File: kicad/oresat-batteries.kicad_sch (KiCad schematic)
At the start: 11 parts, among them J1 J-SAMTEC-TFM-120-X1-XXX-D-RA, SW1 Omron D2F-L3-D (LEFT), SW2 Omron D2F-L3-D (RIGHT), SW3 OMRON D2F-L3-D (LEFT), SW4 OMRON D2F-L3-D (RIGHT)

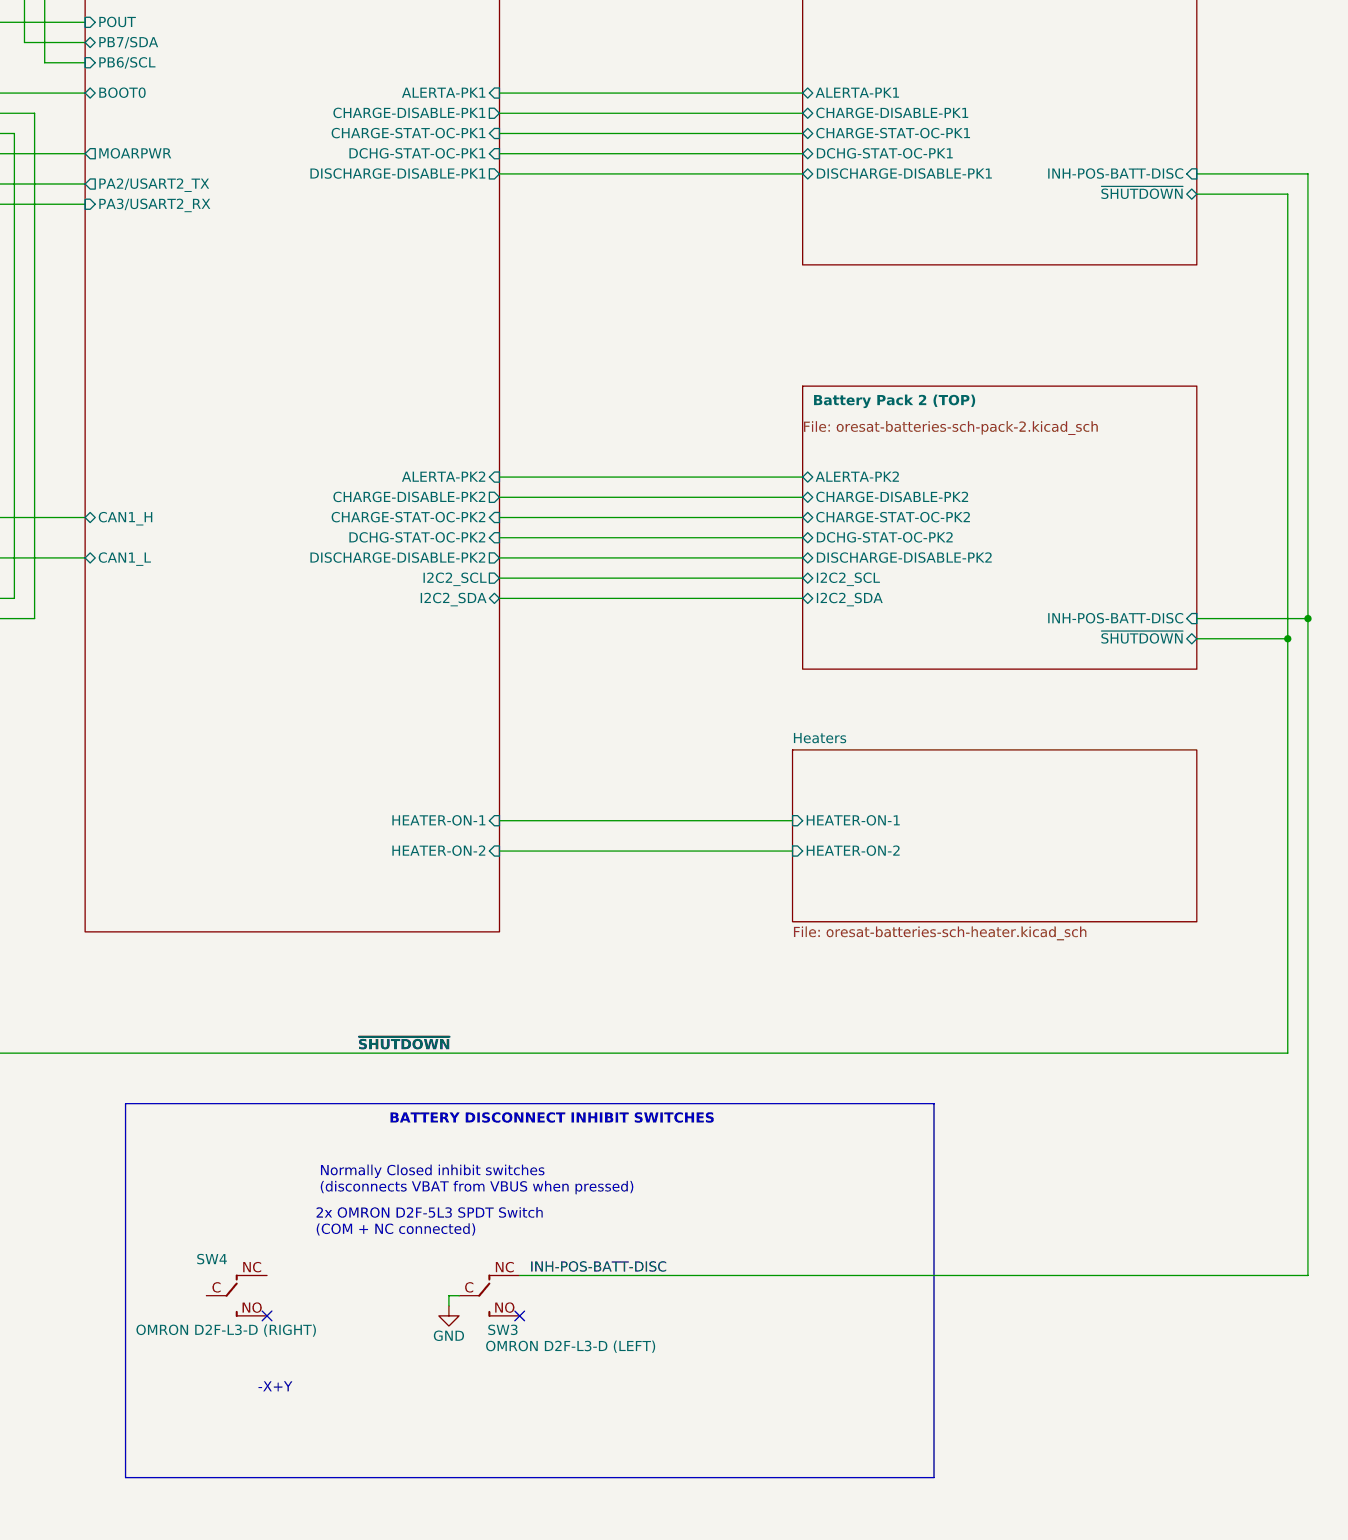
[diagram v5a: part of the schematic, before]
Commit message: Negative battery disconnects in. Ready for KiCad component upgrade.
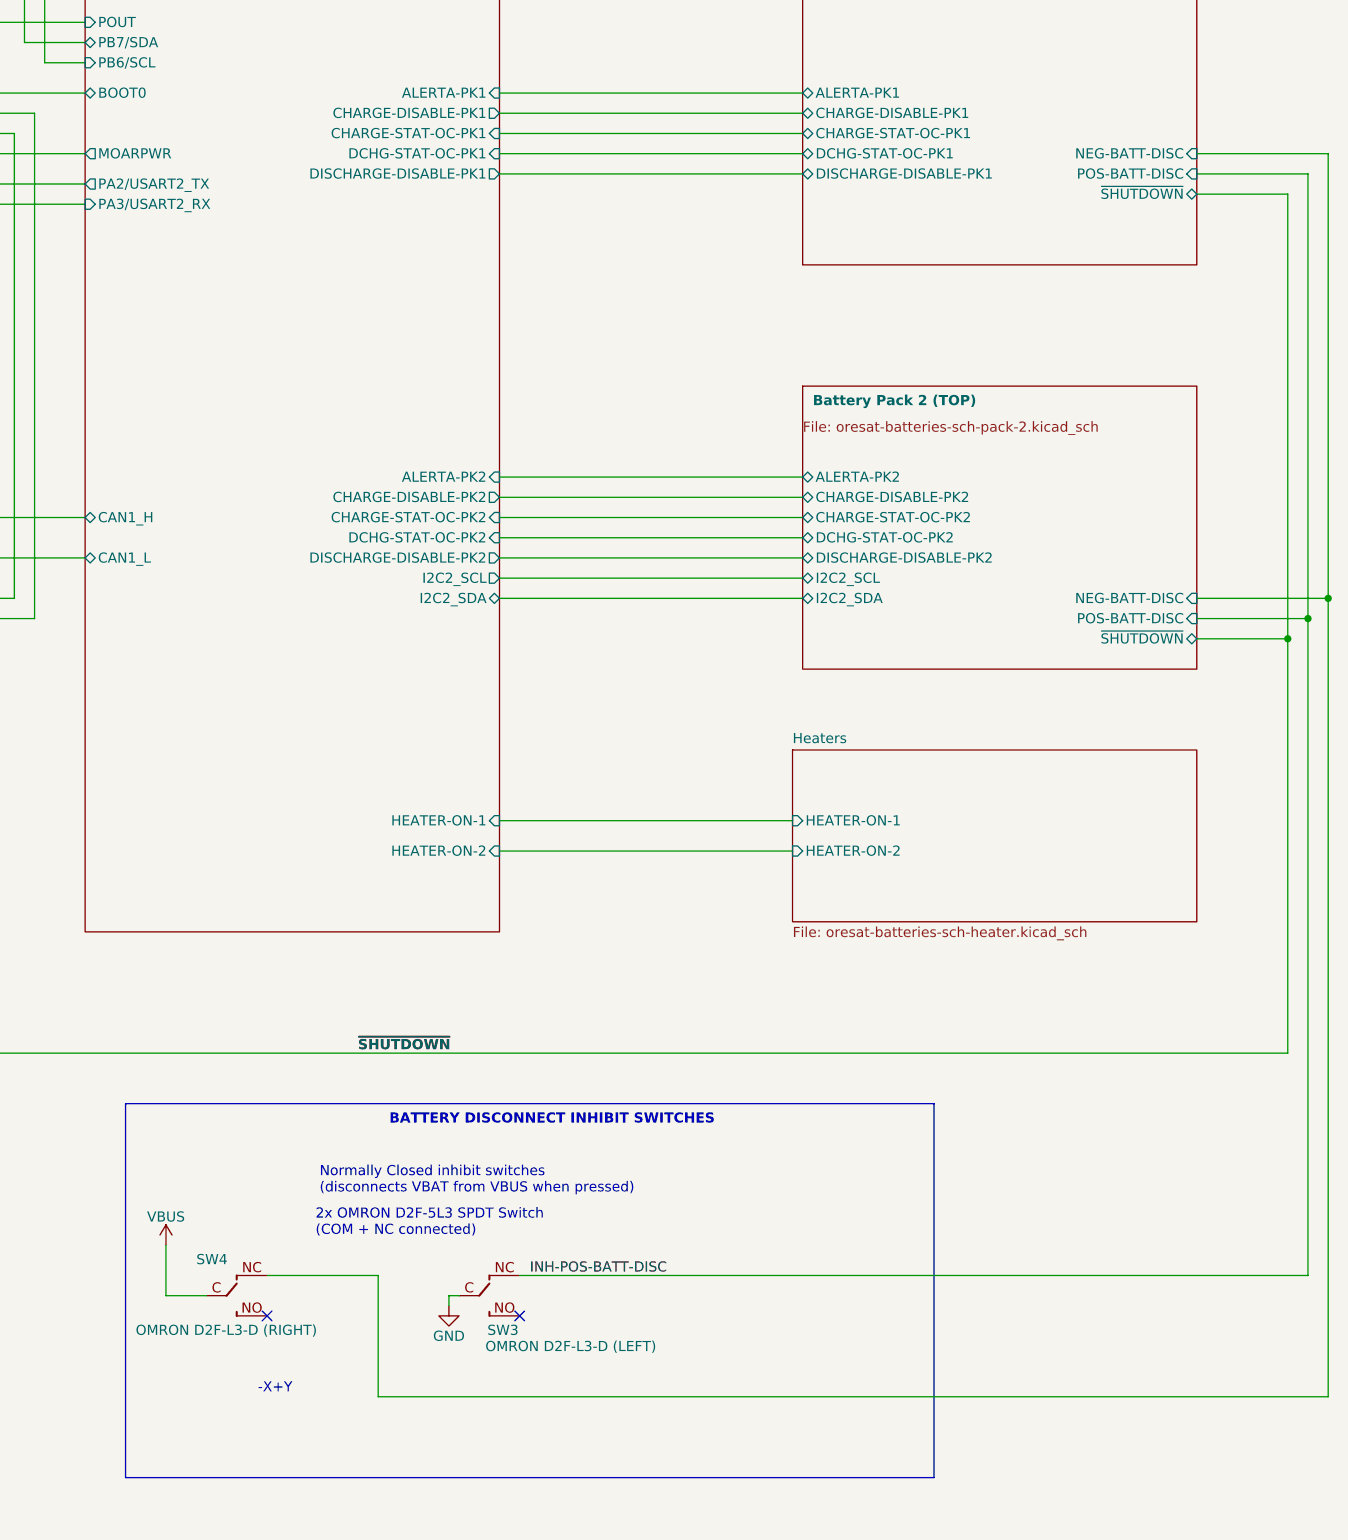
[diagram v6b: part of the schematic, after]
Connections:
- net VBUS: now also SW4.C (COM)
- net Battery Pack 1 (BOTTOM)/NEG-BATT-DISC: now reaches SW4.NC
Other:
- sheet Battery Pack 1 (BOTTOM) ports: added NEG-BATT-DISC, POS-BATT-DISC; removed INH-POS-BATT-DISC
- sheet Battery Pack 2 (TOP) ports: added NEG-BATT-DISC, POS-BATT-DISC; removed INH-POS-BATT-DISC
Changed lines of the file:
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@@
+	)
+	(junction
+		(at 400.05 135.89)
+		(diameter 0)
+		(color 0 0 0 0)
 	)
 	(junction
@@
 	(wire
 		(pts
+			(xy 400.05 236.22) (xy 280.67 236.22)
+		)
+		(stroke
+			(width 0)
+			(type default)
+		)
+	)
+	(wire
+		(pts
 			(xy 191.77 217.17) (xy 213.36 217.17)
 		)
@@
 	(wire
 		(pts
+			(xy 254 217.17) (xy 254 223.52)
+		)
+		(stroke
+			(width 0)
+			(type default)
+		)
+	)
+	(wire
+		(pts
 			(xy 133.35 135.89) (xy 156.21 135.89)
 		)
@@
 	(wire
 		(pts
+			(xy 400.05 135.89) (xy 400.05 236.22)
+		)
+		(stroke
+			(width 0)
+			(type default)
+		)
+	)
+	(wire
+		(pts
 			(xy 135.89 100.33) (xy 143.51 100.33)
 		)
@@
 	(wire
 		(pts
+			(xy 280.67 236.22) (xy 280.67 220.98)
+		)
+		(stroke
+			(width 0)
+			(type default)
+		)
+	)
+	(wire
+		(pts
 			(xy 394.97 193.04) (xy 154.94 193.04)
 		)
@@
 	(wire
 		(pts
+			(xy 254 223.52) (xy 259.08 223.52)
+		)
+		(stroke
+			(width 0)
+			(type default)
+		)
+	)
+	(wire
+		(pts
 			(xy 135.89 74.93) (xy 133.35 74.93)
 		)
@@
 	(wire
 		(pts
+			(xy 383.54 135.89) (xy 400.05 135.89)
+		)
+		(stroke
+			(width 0)
+			(type default)
+		)
+	)
+	(wire
+		(pts
 			(xy 295.91 72.39) (xy 334.01 72.39)
 		)
@@
 	(wire
 		(pts
+			(xy 400.05 80.01) (xy 400.05 135.89)
+		)
+		(stroke
+			(width 0)
+			(type default)
+		)
+	)
+	(wire
+		(pts
 			(xy 232.41 77.47) (xy 234.95 77.47)
 		)
@@
 	(wire
 		(pts
+			(xy 280.67 220.98) (xy 266.7 220.98)
+		)
+		(stroke
+			(width 0)
+			(type default)
+		)
+	)
+	(wire
+		(pts
 			(xy 213.36 217.17) (xy 213.36 227.33)
 		)
@@
 			(width 0.1524)
 			(type solid)
+		)
+	)
+	(wire
+		(pts
+			(xy 383.54 80.01) (xy 400.05 80.01)
+		)
+		(stroke
+			(width 0)
+			(type default)
 		)
 	)
@@
 	)
 	(symbol
+		(lib_id "power:VBUS")
+		(at 254 217.17 0)
+		(unit 1)
+		(exclude_from_sim no)
+		(in_bom yes)
+		(on_board yes)
+		(dnp no)
+		(property "Reference" "#PWR051"
+			(at 254 220.98 0)
+			(effects
+				(font
+					(size 1.27 1.27)
+				)
+				(hide yes)
+			)
+		)
+		(property "Value" "VBUS"
+			(at 254 213.614 0)
+			(effects
+				(font
+					(size 1.27 1.27)
+				)
+			)
+		)
+		(property "Footprint" ""
+			(at 254 217.17 0)
+			(effects
+				(font
+					(size 1.27 1.27)
+				)
+				(hide yes)
+			)
+		)
+		(property "Datasheet" ""
+			(at 254 217.17 0)
+			(effects
+				(font
+					(size 1.27 1.27)
+				)
+				(hide yes)
+			)
+		)
+		(property "Description" "Power symbol creates a global label with name \"VBUS\""
+			(at 254 217.17 0)
+			(effects
+				(font
+					(size 1.27 1.27)
+				)
+				(hide yes)
+			)
+		)
+		(pin "1"
+		)
+		(instances
+			(project "oresat-batteries"
+				(path "/d5070776-2522-4f7b-9d31-10770161e48a"
+					(reference "#PWR051")
+					(unit 1)
+				)
+			)
+		)
+	)
+	(symbol
 		(lib_id "oresat-misc:OMRON-D2F-L3-D-LEFT")
 		(at 294.64 223.52 0)
@@
 			)
 		)
-		(pin "INH-POS-BATT-DISC" input
+		(pin "POS-BATT-DISC" input
 			(at 383.54 138.43 0)
+			(effects
+				(font
+					(size 1.27 1.27)
+				)
+				(justify right)
+			)
+		)
+		(pin "NEG-BATT-DISC" input
+			(at 383.54 135.89 0)
 			(effects
 				(font
@@
 			)
 		)
-		(pin "INH-POS-BATT-DISC" input
+		(pin "POS-BATT-DISC" input
 			(at 383.54 82.55 0)
 			(effects
 				(font
+					(size 1.27 1.27)
+				)
+				(justify right)
+			)
+		)
+		(pin "NEG-BATT-DISC" input
+			(at 383.54 80.01 0)
+			(effects
+				(font

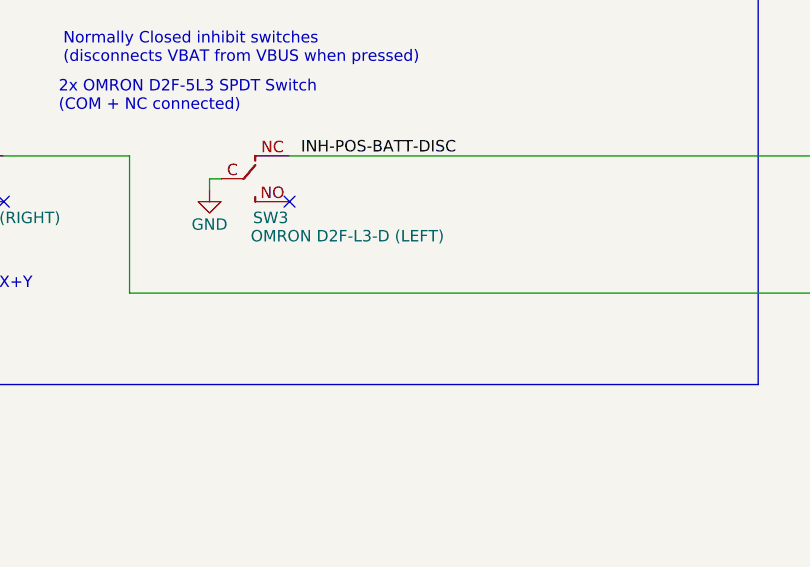
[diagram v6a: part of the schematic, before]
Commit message: Progress on v4
Figure out to bypass negative battery cutoff with 10k to make sure that nSHUTDOWN always works. Lots of moving around (it's tight), finally got pack 1 done. Working on the Pack 2.
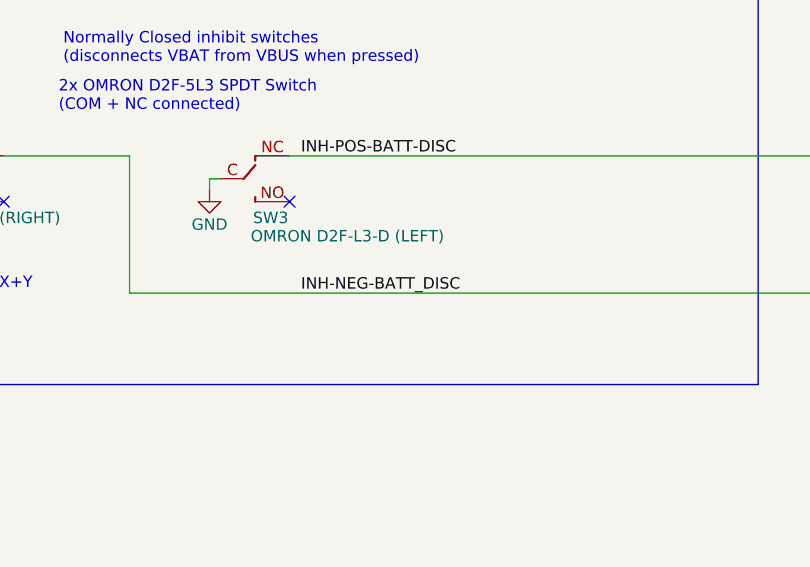
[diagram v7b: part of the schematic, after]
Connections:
- net Battery Pack 1 (BOTTOM)/NEG-BATT-DISC renamed INH-NEG-BATT_DISC
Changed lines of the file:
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@@
+		)
+	)
+	(label "INH-NEG-BATT_DISC"
+		(at 299.72 236.22 0)
+		(effects
+			(font
+				(size 1.27 1.27)
+			)
+			(justify left bottom)
 		)
 	)

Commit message: Progress on battery card v4
Moved in -batt cutoffs, which caused a lot of pain and suffering. Started updating BOM, and fixed all transistor packages. Updated resistor packages, too. Still needs a lot of cleanup, but probably 80% done now.
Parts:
- FIDUCIAL1, FIDUCIAL2, FIDUCIAL3: now left out of the parts list
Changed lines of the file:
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@@
 		(unit 1)
 		(exclude_from_sim no)
-		(in_bom yes)
+		(in_bom no)
 		(on_board yes)
 		(dnp no)
@@
 		(unit 1)
 		(exclude_from_sim no)
-		(in_bom yes)
+		(in_bom no)
 		(on_board yes)
 		(dnp no)
@@
 		(unit 1)
 		(exclude_from_sim no)
-		(in_bom yes)
-		(on_board yes)
-		(dnp no)
+		(in_bom no)
+		(on_board yes)
+		(dnp no)
